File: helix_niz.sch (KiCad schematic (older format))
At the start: 174 parts, among them J1 MJ-4PP-9, P3 OLED, Q1 2SC2712, Q2 2SC2712, SW1 SW_PUSH, SW10 SW_PUSH, SW11 SW_PUSH, SW12 SW_PUSH, SW13 SW_PUSH, SW14 SW_PUSH, SW15 SW_PUSH, SW16 SW_PUSH, SW17 SW_PUSH, SW18 SW_PUSH, SW19 SW_PUSH, SW2 SW_PUSH, SW20 SW_PUSH, SW21 SW_PUSH, SW22 SW_PUSH, SW23 SW_PUSH, SW24 SW_PUSH, SW25 SW_PUSH, SW26 SW_PUSH, SW27 SW_PUSH, SW28 SW_PUSH, SW29 SW_PUSH, SW3 SW_PUSH, SW30 SW_PUSH, SW31 SW_PUSH, SW32 SW_PUSH, SW33 Reset, SW34 SW_PUSH, SW35 SW_PUSH, SW36 SW_PUSH, SW37 SW_PUSH, SW38 SW_PUSH, SW39 SW_PUSH, SW4 SW_PUSH, SW40 SW_PUSH, SW41 SW_PUSH, SW42 SW_PUSH, SW43 SW_PUSH, SW44 SW_PUSH, SW45 SW_PUSH, SW46 SW_PUSH, SW47 SW_PUSH, SW48 SW_PUSH, SW49 SW_PUSH, SW5 SW_PUSH, SW50 SW_PUSH, SW51 SW_PUSH, SW52 SW_PUSH, SW53 SW_PUSH, SW54 SW_PUSH, SW55 SW_PUSH, SW56 SW_PUSH, SW57 SW_PUSH, SW58 SW_PUSH, SW59 SW_PUSH, SW6 SW_PUSH, SW60 SW_PUSH, SW61 SW_PUSH, SW62 SW_PUSH, SW63 SW_PUSH, SW64 SW_PUSH, SW65 SW_PUSH, SW7 SW_PUSH, SW8 SW_PUSH, SW9 SW_PUSH, U1 ProMicro, U34 74HC4051, U35 74HC4051, U36 AD8616, U37 AD8616, U38 ProMicro

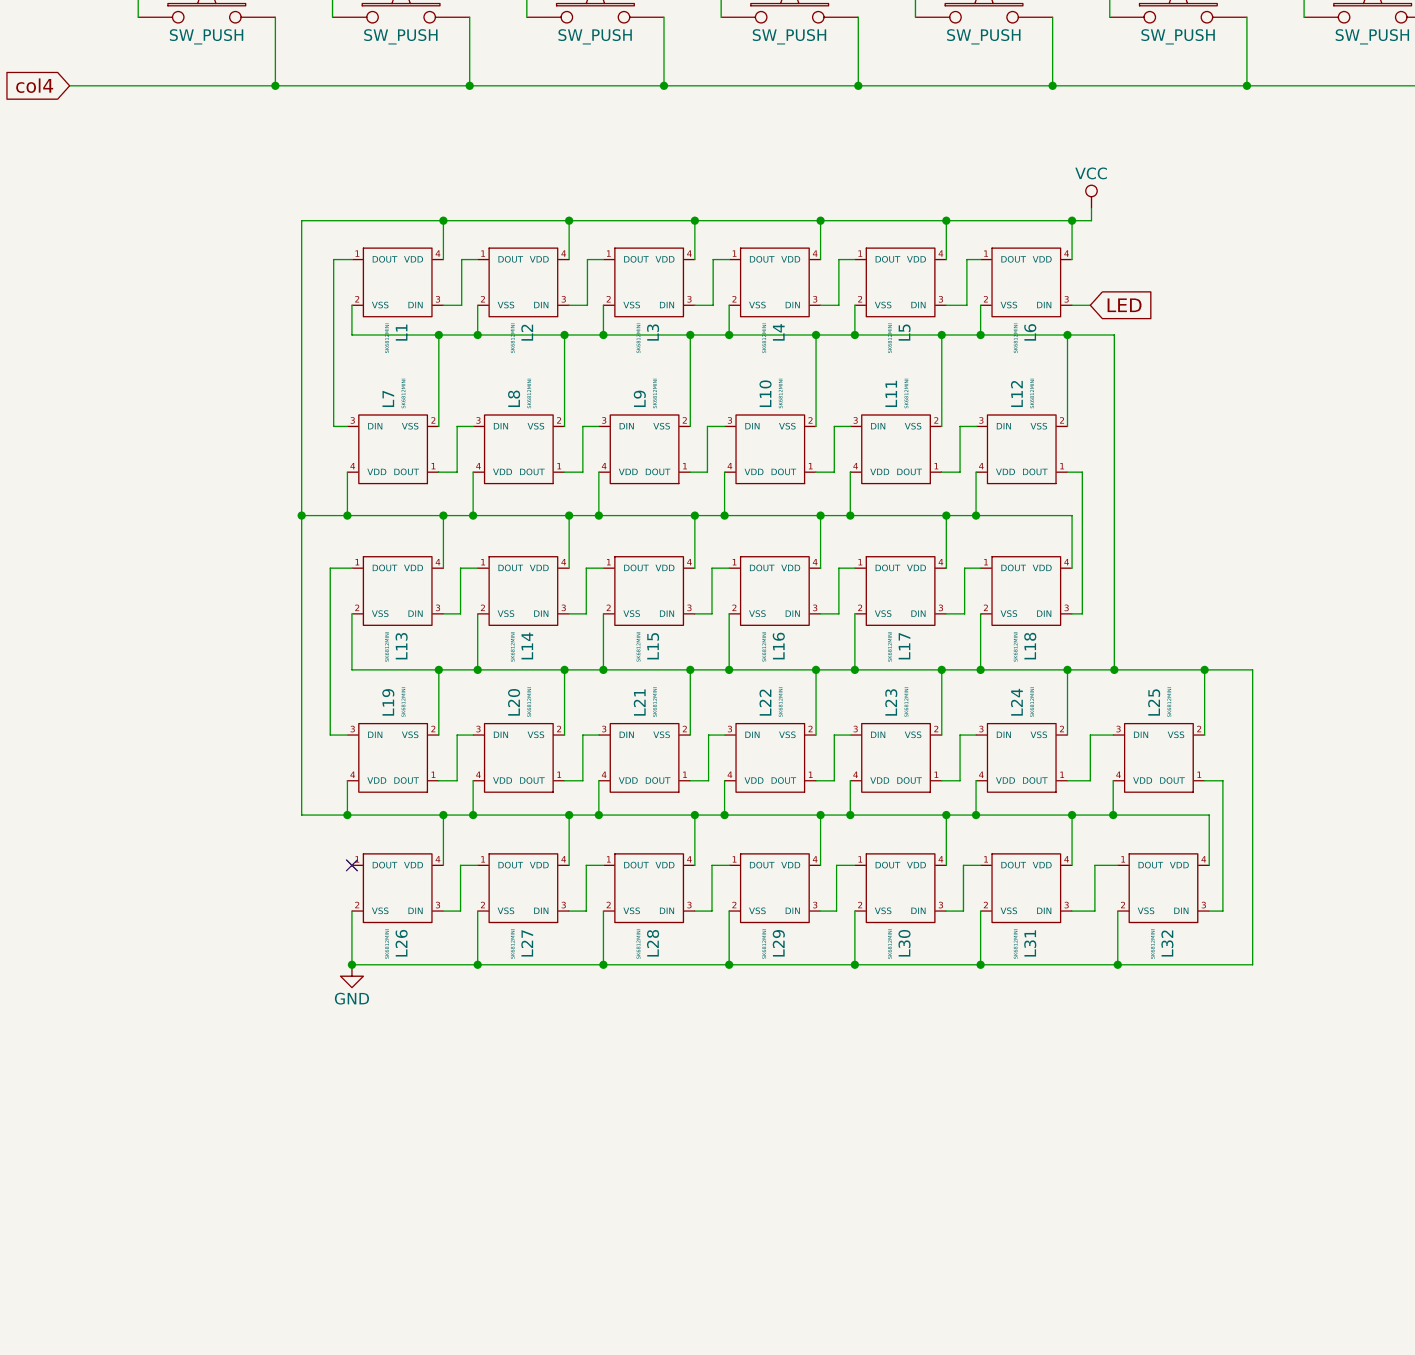
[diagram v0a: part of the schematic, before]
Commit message: ノイズ対策＆nizとvarmiloを同じリポジトリにした
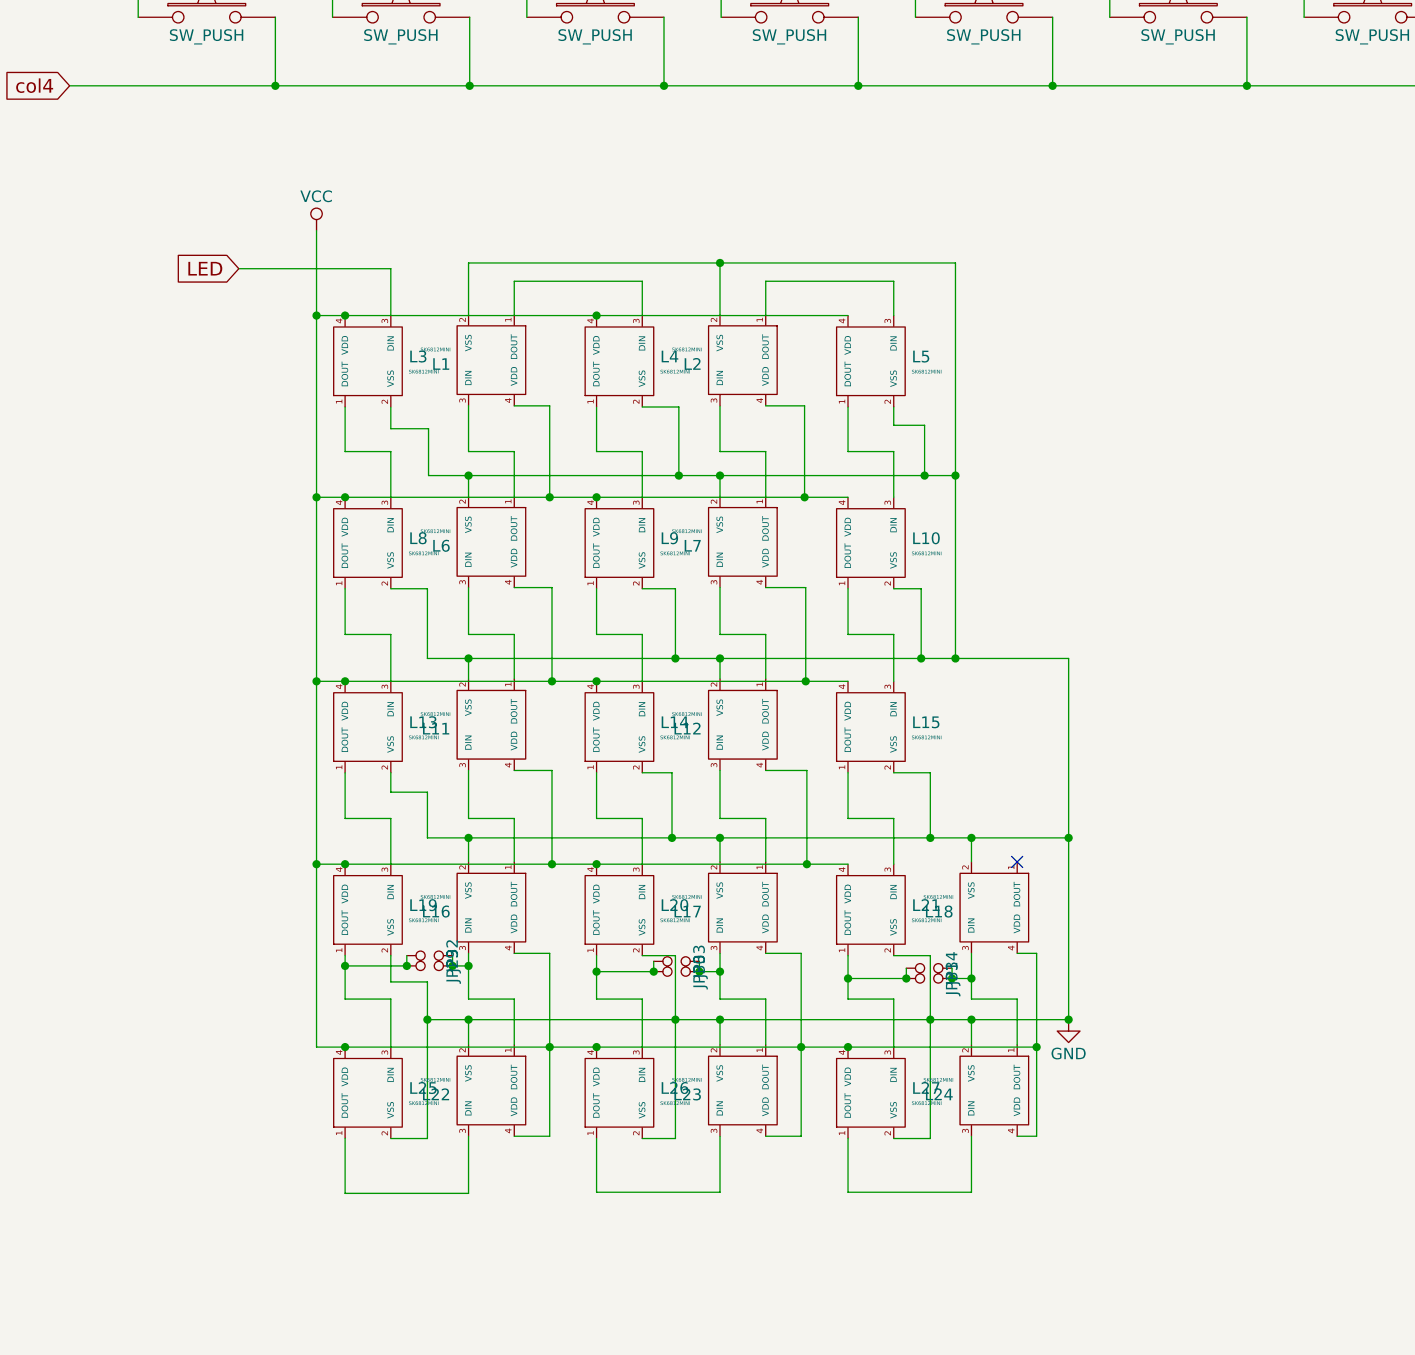
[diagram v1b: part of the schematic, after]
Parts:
- removed L28, L29, L3, L30, L31, L32: SK6812MINI, ec_helix:SK6812MINI_rev, symbol kbd:SK6812MINI
- added JP29, JP30, JP31, JP32, JP33, JP34: GND, kbd:Jumper, symbol Device:Jumper_NO_Small
- added L6: SK6812MINI, ec_helix:SK6812MINI_rev, symbol kbd:SK6812MINI
- renumbered L6 to L3
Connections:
- net GND: now also L6.2 (VSS)
- net VCC: now also L6.4 (VDD)
- net at L3.1 (DOUT): now also L8.3 (DIN); no longer L5.3 (DIN)
- net at L4.3 (DIN): now also L1.1 (DOUT); no longer L5.1 (DOUT)
- net at L4.1 (DOUT): now also L9.3 (DIN)
- net at L2.3 (DIN): now also L7.1 (DOUT)
- net at L1.3 (DIN): now also L6.1 (DOUT); no longer L2.1 (DOUT)
- net at L7.3 (DIN): now also L12.1 (DOUT); no longer L1.1 (DOUT)
- net at L8.1 (DOUT): now also L13.3 (DIN); no longer L9.3 (DIN)
- net at L9.1 (DOUT): now also L14.3 (DIN); no longer L10.3 (DIN)
- net at L11.3 (DIN): now also L16.1 (DOUT); no longer L10.1 (DOUT)
- net at L11.1 (DOUT): now also L6.3 (DIN); no longer L12.3 (DIN)
- net at L18.3 (DIN): now also L24.1 (DOUT), JP31.2, JP34.2; no longer L12.1 (DOUT)
- net at L17.3 (DIN): now also L23.1 (DOUT), JP30.2, JP33.2; no longer L18.1 (DOUT)
- net at L16.3 (DIN): now also L22.1 (DOUT), JP29.2, JP32.2; no longer L17.1 (DOUT)
- net at L15.3 (DIN): now also L10.1 (DOUT); no longer L16.1 (DOUT)
- net at L15.1 (DOUT): now also L21.3 (DIN); no longer L14.3 (DIN)
- net at L14.1 (DOUT): now also L20.3 (DIN); no longer L13.3 (DIN)
- net at L19.1 (DOUT): now also L25.3 (DIN), JP29.1, JP32.1; no longer L20.3 (DIN)
- net at L20.1 (DOUT): now also L26.3 (DIN), JP30.1, JP33.1; no longer L21.3 (DIN)
- net at L22.3 (DIN): now also L25.1 (DOUT); no longer L21.1 (DOUT)
- net at L23.3 (DIN): now also L26.1 (DOUT); no longer L22.1 (DOUT)
- net at L24.3 (DIN): now also L27.1 (DOUT); no longer L23.1 (DOUT)
- net at L27.3 (DIN): now also L21.1 (DOUT), JP31.1, JP34.1
- new net: L10.3 (DIN), L5.1 (DOUT)
- new net: L2.1 (DOUT), L5.3 (DIN)
- new net: L12.3 (DIN), L17.1 (DOUT)
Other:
- moved on the sheet: L3
